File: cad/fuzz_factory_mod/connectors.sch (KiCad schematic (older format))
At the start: 12 parts

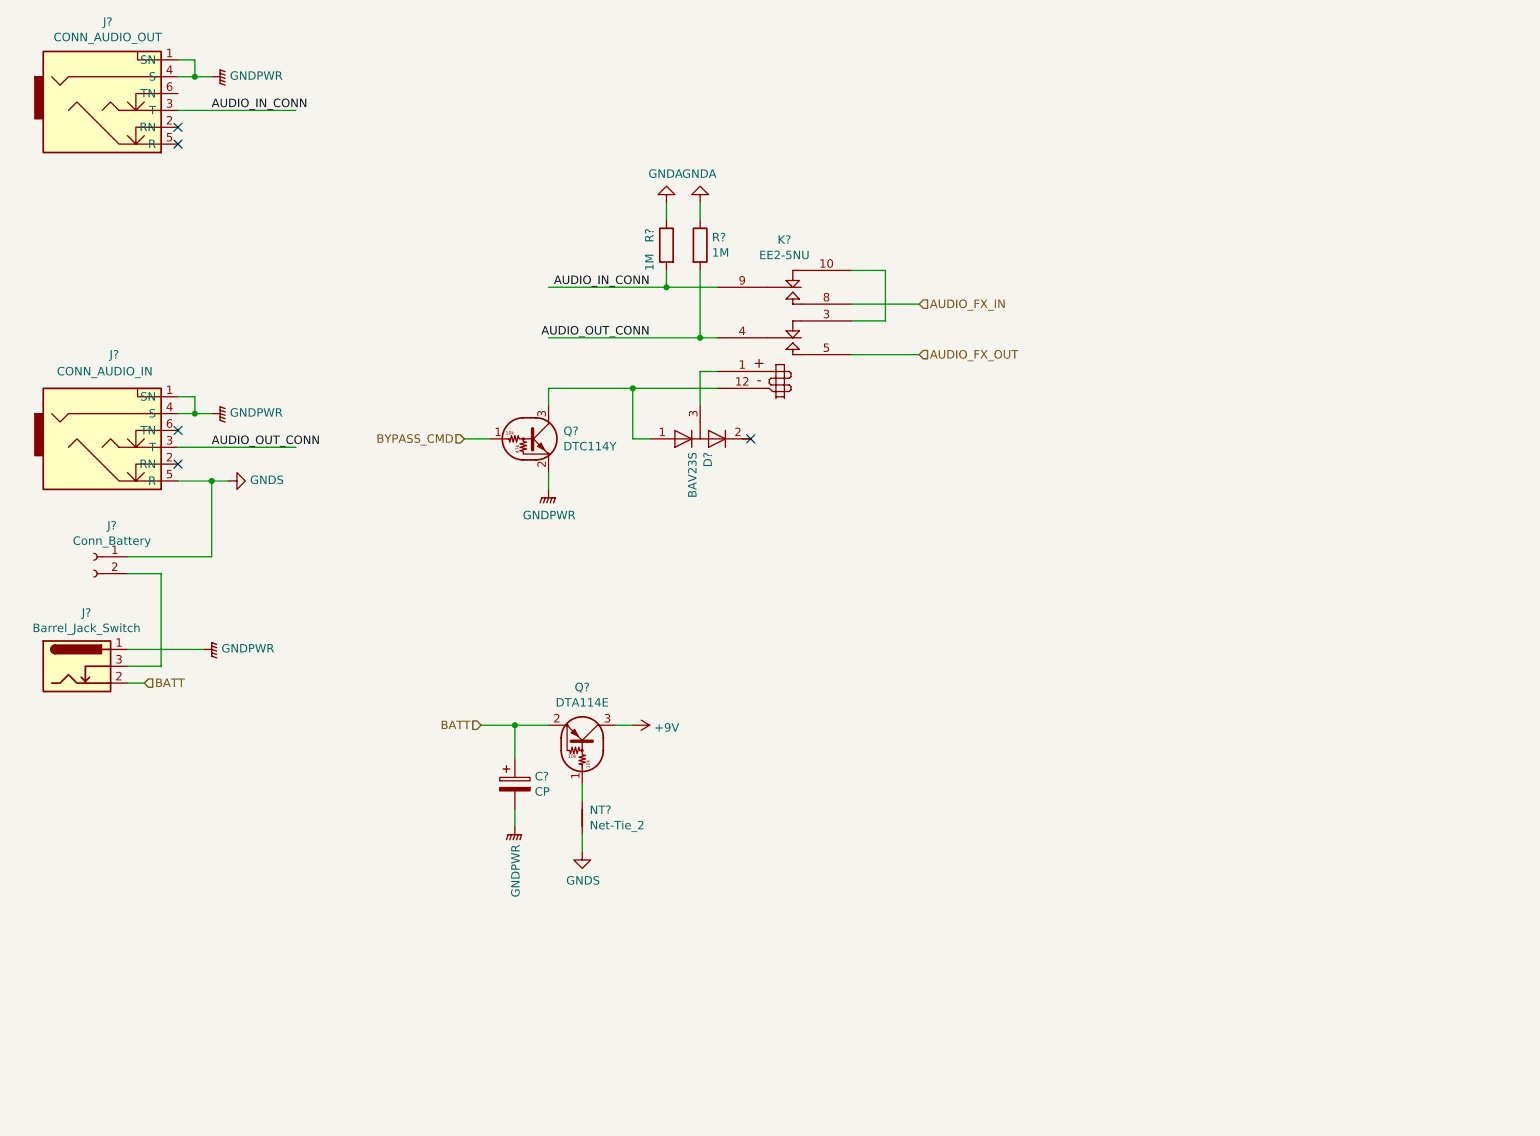
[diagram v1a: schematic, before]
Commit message: Continued schematic.
Modified fuuz_factory circuit : use of matched transistor pairs.
Added USB interface, through FT230X and direct to MCU.
Associated footprints, except for XTAL and trimmers.
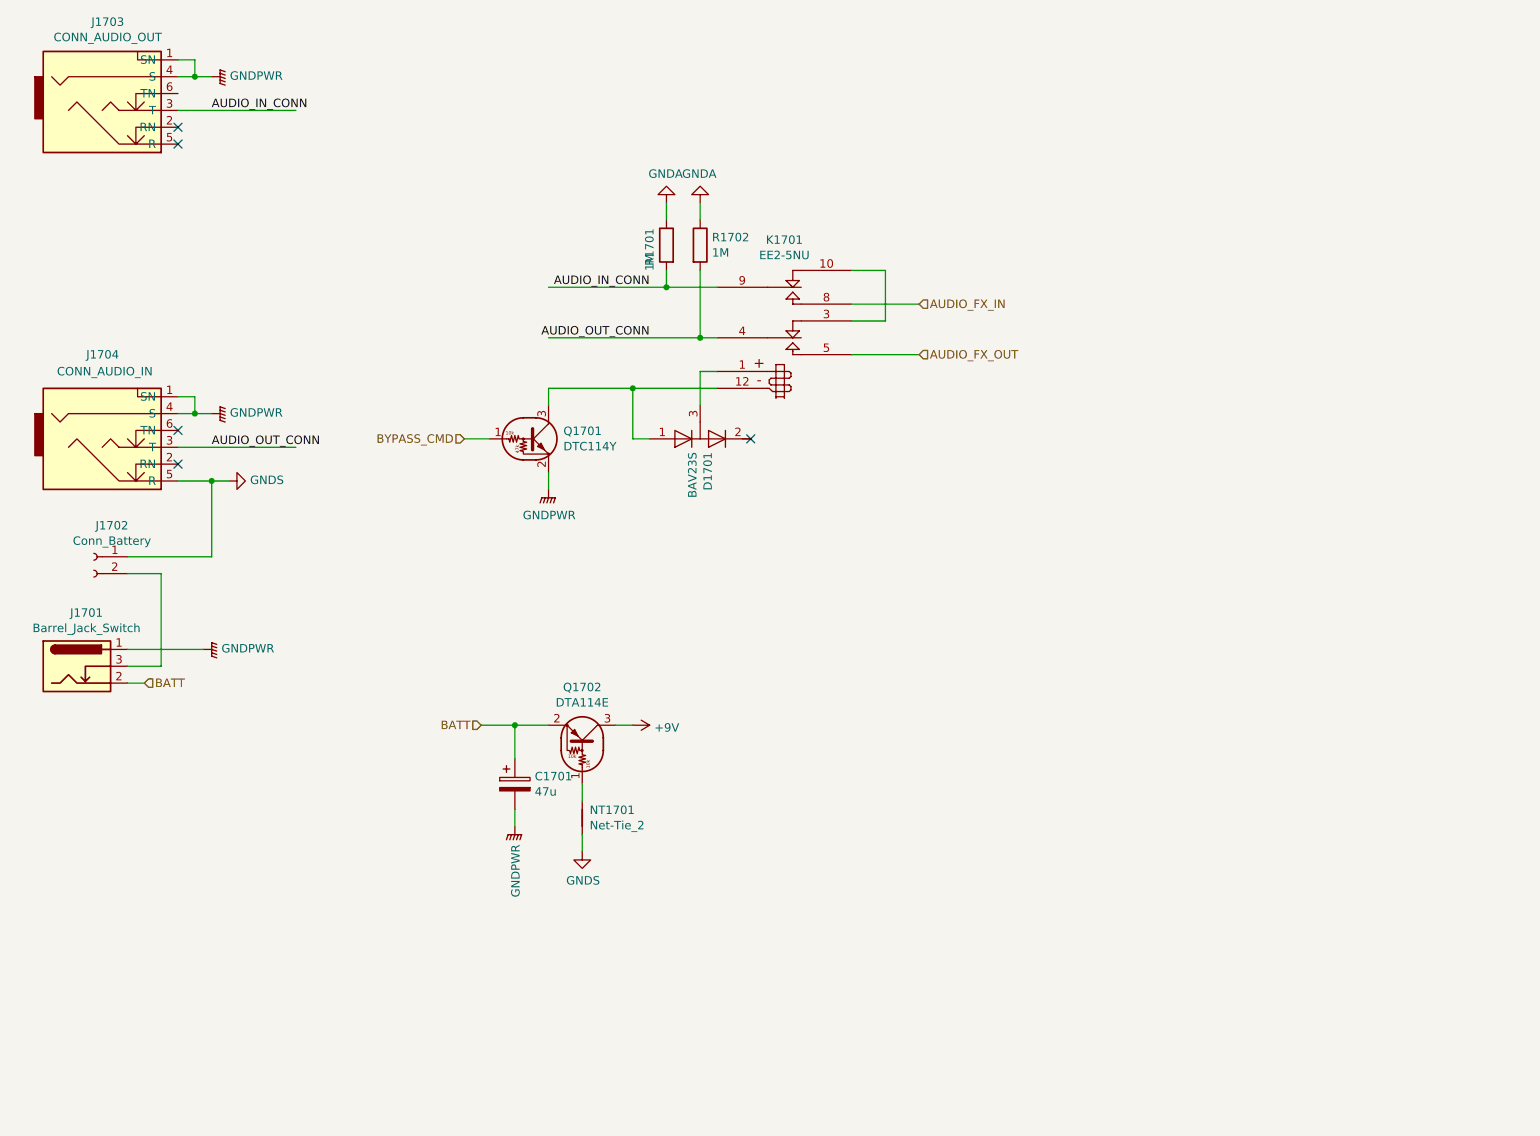
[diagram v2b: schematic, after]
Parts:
- C1701: renamed from C?; value CP -> 47u; footprint (none) -> Capacitors_SMD:CP_Elec_6.3x4.5
- D1701: renamed from D?; footprint (none) -> TO_SOT_Packages_SMD:SOT-23
- J1701: renamed from J?; footprint (none) -> Connect:JACK_ALIM
- J1702: renamed from J?; footprint (none) -> Pin_Headers:Pin_Header_Straight_1x02_Pitch2.54mm
- J1703, J1704: renamed from J?; footprint (none) -> Connect:NMJ6HCD2
- K1701: renamed from K?; footprint (none) -> flax_lib:RELAY-EE2
- NT1701: renamed from NT?; footprint (none) -> Oddities:NetTie-II
- Q1701, Q1702: renamed from Q?; footprint (none) -> TO_SOT_Packages_SMD:SOT-23
- R1701, R1702: renamed from R?; footprint (none) -> Resistors_SMD:R_0603
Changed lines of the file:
@@
 $Descr A4 11693 8268
 encoding utf-8
-Sheet 7 19
+Sheet 16 22
 Title ""
 Date ""
@@
 $EndDescr
 $Comp
-L flax_lib:EE2-5NU K?
+L flax_lib:EE2-5NU K1701
 U 1 1 5DE5A46A
 P 6400 2650
-F 0 "K?" H 6400 3181 50  0000 C CNN
+F 0 "K1701" H 6400 3181 50  0000 C CNN
 F 1 "EE2-5NU" H 6400 3090 50  0000 C CNN
-F 2 "" H 6400 2650 50  0000 C CNN
+F 2 "flax_lib:RELAY-EE2" H 6400 2650 50  0001 C CNN
 F 3 "" H 6400 2650 50  0000 C CNN
 	1    6400 2650
@@
 $EndComp
 $Comp
-L flax_lib:CLIFF_FCR50051 J?
+L flax_lib:CLIFF_FCR50051 J1703
 U 1 1 5DE5BD43
 P 2400 1350
-F 0 "J?" H 2383 1875 50  0000 C CNN
+F 0 "J1703" H 2383 1875 50  0000 C CNN
 F 1 "CONN_AUDIO_OUT" H 2383 1784 50  0000 C CNN
-F 2 "" H 2500 1200 50  0001 C CNN
+F 2 "Connect:NMJ6HCD2" H 2500 1200 50  0001 C CNN
 F 3 "" H 2500 1200 50  0001 C CNN
 	1    2400 1350
@@
 $EndComp
 $Comp
-L flax_lib:CLIFF_FCR50051 J?
+L flax_lib:CLIFF_FCR50051 J1704
 U 1 1 5DE5C90E
 P 2400 3350
-F 0 "J?" H 2450 3900 50  0000 R CNN
+F 0 "J1704" H 2450 3900 50  0000 R CNN
 F 1 "CONN_AUDIO_IN" H 2650 3800 50  0000 R CNN
-F 2 "" H 2500 3200 50  0001 C CNN
+F 2 "Connect:NMJ6HCD2" H 2500 3200 50  0001 C CNN
 F 3 "" H 2500 3200 50  0001 C CNN
 	1    2400 3350
@@
 $EndComp
 $Comp
-L Transistor_BJT:DTC114Y Q?
+L Transistor_BJT:DTC114Y Q1701
 U 1 1 5DE5E2B7
 P 4900 3300
-F 0 "Q?" H 5088 3346 50  0000 L CNN
+F 0 "Q1701" H 5088 3346 50  0000 L CNN
 F 1 "DTC114Y" H 5088 3255 50  0000 L CNN
-F 2 "" H 4900 3300 50  0001 L CNN
+F 2 "TO_SOT_Packages_SMD:SOT-23" H 4900 3300 50  0001 L CNN
 F 3 "" H 4900 3300 50  0001 L CNN
 	1    4900 3300
@@
 $EndComp
 $Comp
-L flax_lib:BAV23S D?
+L flax_lib:BAV23S D1701
 U 1 1 5DE5F68B
 P 5900 3300
-F 0 "D?" V 5946 3379 50  0000 L CNN
+F 0 "D1701" V 5946 3379 50  0000 L CNN
 F 1 "BAV23S" V 5855 3379 50  0000 L CNN
-F 2 "" H 5900 3300 50  0001 C CNN
+F 2 "TO_SOT_Packages_SMD:SOT-23" H 5900 3300 50  0001 C CNN
 F 3 "" H 5900 3300 50  0001 C CNN
 	1    5900 3300
@@
 $EndComp
 $Comp
-L Connector:Barrel_Jack_Switch J?
+L Connector:Barrel_Jack_Switch J1701
 U 1 1 5DE61D3B
 P 2200 4650
-F 0 "J?" H 2257 4967 50  0000 C CNN
+F 0 "J1701" H 2257 4967 50  0000 C CNN
 F 1 "Barrel_Jack_Switch" H 2257 4876 50  0000 C CNN
-F 2 "" H 2250 4610 50  0001 C CNN
+F 2 "Connect:JACK_ALIM" H 2250 4610 50  0001 C CNN
 F 3 "~" H 2250 4610 50  0001 C CNN
 	1    2200 4650
@@
 	7000 2300 6800 2300
 $Comp
-L power:GNDPWR #PWR?
+L power:GNDPWR #PWR01706
 U 1 1 5E049671
 P 5000 3600
-F 0 "#PWR?" H 5000 3400 50  0001 C CNN
+F 0 "#PWR01706" H 5000 3400 50  0001 C CNN
 F 1 "GNDPWR" H 5004 3446 50  0000 C CNN
 F 2 "" H 5000 3550 50  0001 C CNN
@@
 	4650 3300 4500 3300
 $Comp
-L Device:R R?
+L Device:R R1702
 U 1 1 5E0563EF
 P 5900 2150
-F 0 "R?" H 5970 2196 50  0000 L CNN
+F 0 "R1702" H 5970 2196 50  0000 L CNN
 F 1 "1M" H 5970 2105 50  0000 L CNN
-F 2 "" V 5830 2150 50  0001 C CNN
+F 2 "Resistors_SMD:R_0603" V 5830 2150 50  0001 C CNN
 F 3 "~" H 5900 2150 50  0001 C CNN
 	1    5900 2150
@@
 $EndComp
 $Comp
-L Device:R R?
+L Device:R R1701
 U 1 1 5E056DB3
 P 5700 2150
-F 0 "R?" V 5800 2250 50  0000 R CNN
+F 0 "R1701" V 5800 2250 50  0000 R CNN
 F 1 "1M" V 5800 2100 50  0000 R CNN
-F 2 "" V 5630 2150 50  0001 C CNN
+F 2 "Resistors_SMD:R_0603" V 5630 2150 50  0001 C CNN
 F 3 "~" H 5700 2150 50  0001 C CNN
 	1    5700 2150
@@
 	5700 2400 6000 2400
 $Comp
-L power:GNDA #PWR?
+L power:GNDA #PWR01710
 U 1 1 5E058766
 P 5900 1900
-F 0 "#PWR?" H 5900 1650 50  0001 C CNN
+F 0 "#PWR01710" H 5900 1650 50  0001 C CNN
 F 1 "GNDA" H 5905 1727 50  0000 C CNN
 F 2 "" H 5900 1900 50  0001 C CNN
@@
 $EndComp
 $Comp
-L power:GNDA #PWR?
+L power:GNDA #PWR01709
 U 1 1 5E059243
 P 5700 1900
-F 0 "#PWR?" H 5700 1650 50  0001 C CNN
+F 0 "#PWR01709" H 5700 1650 50  0001 C CNN
 F 1 "GNDA" H 5705 1727 50  0000 C CNN
 F 2 "" H 5700 1900 50  0001 C CNN
@@
 	2600 4750 2500 4750
 $Comp
-L power:GNDPWR #PWR?
+L power:GNDPWR #PWR01703
 U 1 1 5E333C4B
 P 3000 3150
-F 0 "#PWR?" H 3000 2950 50  0001 C CNN
+F 0 "#PWR01703" H 3000 2950 50  0001 C CNN
 F 1 "GNDPWR" V 3005 3042 50  0000 R CNN
 F 2 "" H 3000 3100 50  0001 C CNN
@@
 	2800 3350 3500 3350
 $Comp
-L Connector:Conn_01x02_Female J?
+L Connector:Conn_01x02_Female J1702
 U 1 1 5E3469C4
 P 2300 4000
-F 0 "J?" H 2192 4185 50  0000 C CNN
+F 0 "J1702" H 2192 4185 50  0000 C CNN
 F 1 "Conn_Battery" H 2192 4094 50  0000 C CNN
-F 2 "" H 2300 4000 50  0001 C CNN
+F 2 "Pin_Headers:Pin_Header_Straight_1x02_Pitch2.54mm" H 2300 4000 50  0001 C CNN
 F 3 "~" H 2300 4000 50  0001 C CNN
 	1    2300 4000
@@
 	2800 3150 2900 3150
 $Comp
-L power:GNDPWR #PWR?
+L power:GNDPWR #PWR01701
 U 1 1 5E34C9B1
 P 2950 4550
-F 0 "#PWR?" H 2950 4350 50  0001 C CNN
+F 0 "#PWR01701" H 2950 4350 50  0001 C CNN
 F 1 "GNDPWR" V 2955 4442 50  0000 R CNN
 F 2 "" H 2950 4500 50  0001 C CNN
@@
 	2900 3150 3000 3150
 $Comp
-L power:GNDPWR #PWR?
+L power:GNDPWR #PWR01702
 U 1 1 5E34F5E8
 P 3000 1150
-F 0 "#PWR?" H 3000 950 50  0001 C CNN
+F 0 "#PWR01702" H 3000 950 50  0001 C CNN
 F 1 "GNDPWR" V 3005 1042 50  0000 R CNN
 F 2 "" H 3000 1100 50  0001 C CNN
@@
 	5000 2400 5700 2400
 $Comp
-L Transistor_BJT:DTA114E Q?
+L Transistor_BJT:DTA114E Q1702
 U 1 1 5E6CC80A
 P 5200 5100
-F 0 "Q?" V 5525 5100 50  0000 C CNN
+F 0 "Q1702" V 5525 5100 50  0000 C CNN
 F 1 "DTA114E" V 5434 5100 50  0000 C CNN
-F 2 "" H 5200 5100 50  0001 L CNN
+F 2 "TO_SOT_Packages_SMD:SOT-23" H 5200 5100 50  0001 L CNN
 F 3 "" H 5200 5100 50  0001 L CNN
 	1    5200 5100
@@
 $EndComp
 $Comp
-L Device:CP C?
+L Device:CP C1701
 U 1 1 5E6D0A71
 P 4800 5350
-F 0 "C?" H 4918 5396 50  0000 L CNN
-F 1 "CP" H 4918 5305 50  0000 L CNN
-F 2 "" H 4838 5200 50  0001 C CNN
+F 0 "C1701" H 4918 5396 50  0000 L CNN
+F 1 "47u" H 4918 5305 50  0000 L CNN
+F 2 "Capacitors_SMD:CP_Elec_6.3x4.5" H 4838 5200 50  0001 C CNN
 F 3 "~" H 4800 5350 50  0001 C CNN
 	1    4800 5350
@@
 	4800 5000 4600 5000
 $Comp
-L power:GNDS #PWR?
+L power:GNDS #PWR01707
 U 1 1 5E6D3A5E
 P 5200 5750
-F 0 "#PWR?" H 5200 5500 50  0001 C CNN
+F 0 "#PWR01707" H 5200 5500 50  0001 C CNN
 F 1 "GNDS" H 5205 5577 50  0000 C CNN
 F 2 "" H 5200 5750 50  0001 C CNN
@@
 $EndComp
 $Comp
-L power:GNDS #PWR?
+L power:GNDS #PWR01704
 U 1 1 5E6D5175
 P 3100 3550
-F 0 "#PWR?" H 3100 3300 50  0001 C CNN
+F 0 "#PWR01704" H 3100 3300 50  0001 C CNN
 F 1 "GNDS" V 3105 3422 50  0000 R CNN
 F 2 "" H 3100 3550 50  0001 C CNN
@@
 Connection ~ 3000 3550
 $Comp
-L power:GNDPWR #PWR?
+L power:GNDPWR #PWR01705
 U 1 1 5E6D6DCD
 P 4800 5600
-F 0 "#PWR?" H 4800 5400 50  0001 C CNN
+F 0 "#PWR01705" H 4800 5400 50  0001 C CNN
 F 1 "GNDPWR" V 4805 5492 50  0000 R CNN
 F 2 "" H 4800 5550 50  0001 C CNN
@@
 	4800 5500 4800 5600
 $Comp
-L power:+9V #PWR?
+L power:+9V #PWR01708
 U 1 1 5E6D8A78
 P 5500 5000
-F 0 "#PWR?" H 5500 4850 50  0001 C CNN
+F 0 "#PWR01708" H 5500 4850 50  0001 C CNN
 F 1 "+9V" V 5515 5128 50  0000 L CNN
 F 2 "" H 5500 5000 50  0001 C CNN
@@
 	5500 5000 5400 5000
 $Comp
-L Device:Net-Tie_2 NT?
+L Device:Net-Tie_2 NT1701
 U 1 1 5E6DBA2F
 P 5200 5550
-F 0 "NT?" V 5154 5594 50  0000 L CNN
+F 0 "NT1701" V 5154 5594 50  0000 L CNN
 F 1 "Net-Tie_2" V 5245 5594 50  0000 L CNN
-F 2 "" H 5200 5550 50  0001 C CNN
+F 2 "Oddities:NetTie-II" H 5200 5550 50  0001 C CNN
 F 3 "~" H 5200 5550 50  0001 C CNN
 	1    5200 5550
